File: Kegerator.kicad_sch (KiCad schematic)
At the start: 17 parts, among them J1 Buttons, J2 LCD, J3 Temperature, J4 Programmer, J5 Control, U1 ESP32-S2-WROVER, U2 MCP1700

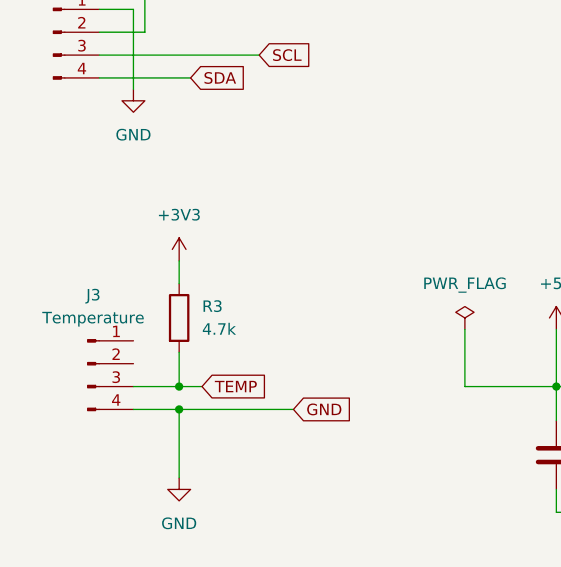
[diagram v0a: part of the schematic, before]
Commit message: Allowing the temperature sensor to be able to be both really powered or parasitic power
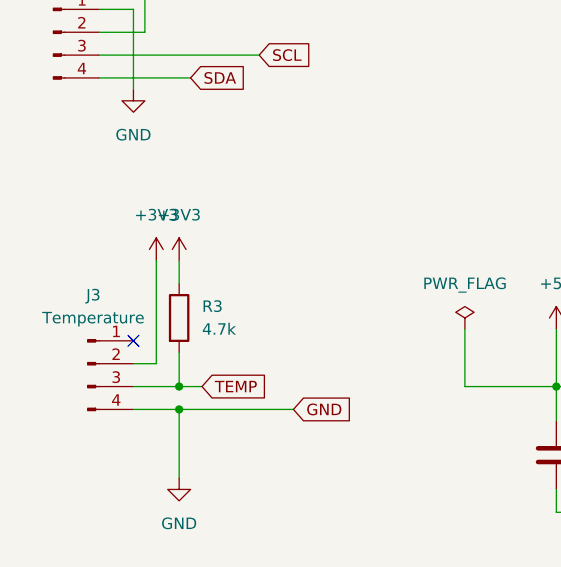
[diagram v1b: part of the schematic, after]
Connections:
- net +3V3: now also J3.2 (Pin_2)
- no-connect marks 27 -> 28
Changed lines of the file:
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@@
+	)
+	(no_connect
+		(at 60.96 138.43)
 	)
 	(no_connect
@@
 	(wire
 		(pts
+			(xy 60.96 140.97) (xy 63.5 140.97)
+		)
+		(stroke
+			(width 0)
+			(type default)
+		)
+	)
+	(wire
+		(pts
 			(xy 243.84 40.64) (xy 260.35 40.64)
 		)
@@
 		(pts
 			(xy 119.38 44.45) (xy 137.16 44.45)
+		)
+		(stroke
+			(width 0)
+			(type default)
+		)
+	)
+	(wire
+		(pts
+			(xy 63.5 140.97) (xy 63.5 129.54)
 		)
 		(stroke
@@
 					(unit 1)
 				)
+			)
+		)
+	)
+	(symbol
+		(lib_id "power:+3V3")
+		(at 63.5 129.54 0)
+		(unit 1)
+		(exclude_from_sim no)
+		(in_bom yes)
+		(on_board yes)
+		(dnp no)
+		(fields_autoplaced yes)
+		(property "Reference" "#PWR013"
+			(at 63.5 133.35 0)
+			(effects
+				(font
+					(size 1.27 1.27)
+				)
+				(hide yes)
+			)
+		)
+		(property "Value" "+3V3"
+			(at 63.5 124.46 0)
+			(effects
+				(font
+					(size 1.27 1.27)
+				)
+			)
+		)
+		(property "Footprint" ""
+			(at 63.5 129.54 0)
+			(effects
+				(font
+					(size 1.27 1.27)
+				)
+				(hide yes)
+			)
+		)
+		(property "Datasheet" ""
+			(at 63.5 129.54 0)
+			(effects
+				(font
+					(size 1.27 1.27)
+				)
+				(hide yes)
+			)
+		)
+		(property "Description" "Power symbol creates a global label with name \"+3V3\""
+			(at 63.5 129.54 0)
+			(effects
+				(font
+					(size 1.27 1.27)
+				)
+				(hide yes)
+			)
+		)
+		(pin "1"
+		)
+		(instances
+			(project "Kegerator"
+				(path "/0d8fcf03-5d01-4d3e-974a-da58a94c5b7b"
+					(reference "#PWR013")
+					(unit 1)
+				)

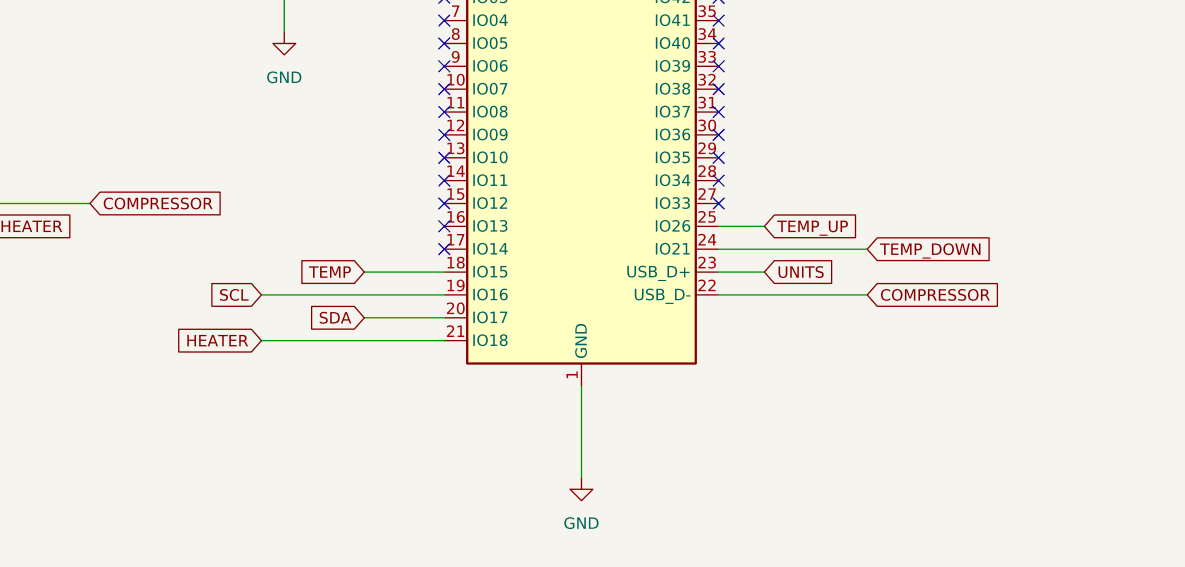
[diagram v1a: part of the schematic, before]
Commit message: STop using GPIO26
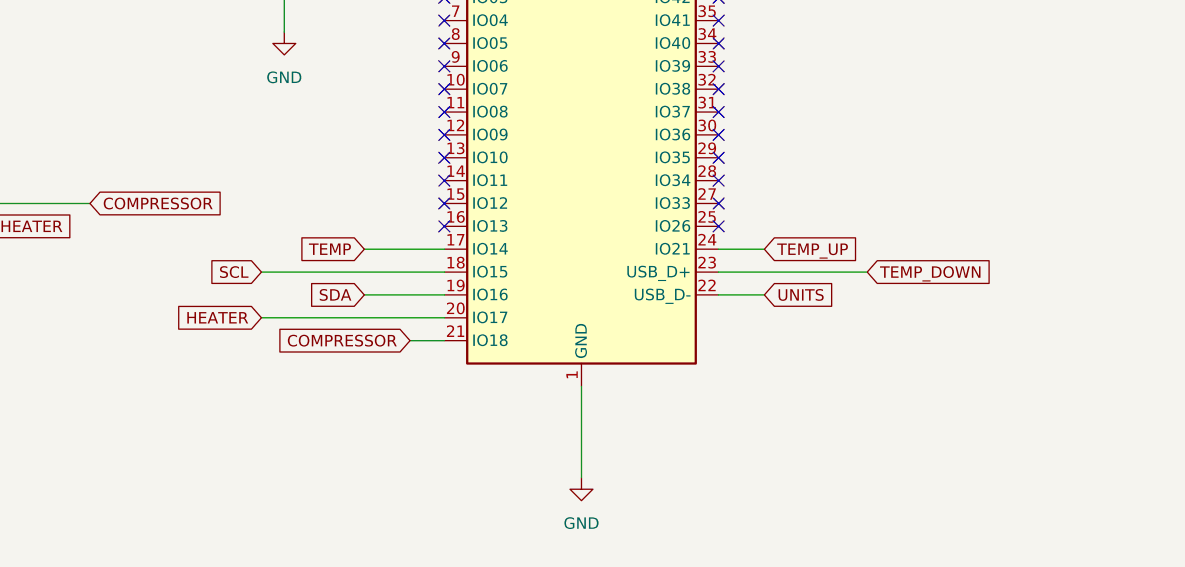
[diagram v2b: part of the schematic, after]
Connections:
- net COMPRESSOR: now also U1.21 (IO18); no longer U1.22 (USB_D-)
- net HEATER: now also U1.20 (IO17); no longer U1.21 (IO18)
- net SCL: now also U1.18 (IO15); no longer U1.19 (IO16)
- net SDA: now also U1.19 (IO16); no longer U1.20 (IO17)
- net TEMP: now also U1.17 (IO14); no longer U1.18 (IO15)
- net TEMP_DOWN: now also U1.23 (USB_D+); no longer U1.24 (IO21)
- net TEMP_UP: now also U1.24 (IO21); no longer U1.25 (IO26)
- net UNITS: now also U1.22 (USB_D-); no longer U1.23 (USB_D+)
